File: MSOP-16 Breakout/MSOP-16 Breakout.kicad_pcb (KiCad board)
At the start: 2 copper layers, 3 parts, among them J1 Conn_01x08_Male, J2 Conn_01x08_Male, U1 LTC6820

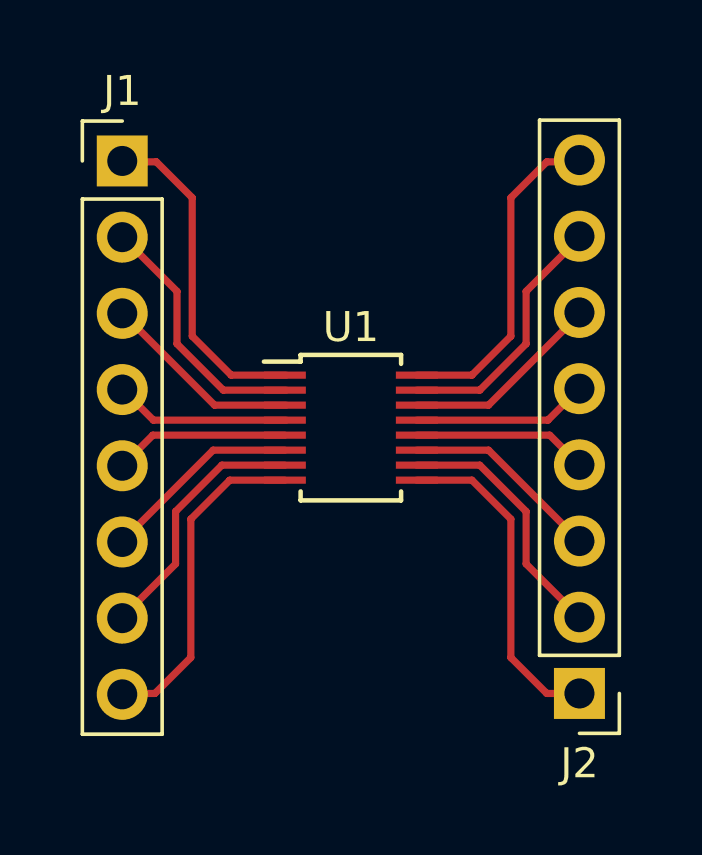
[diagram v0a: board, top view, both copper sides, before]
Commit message: Update BMS bias resistors and enable pin
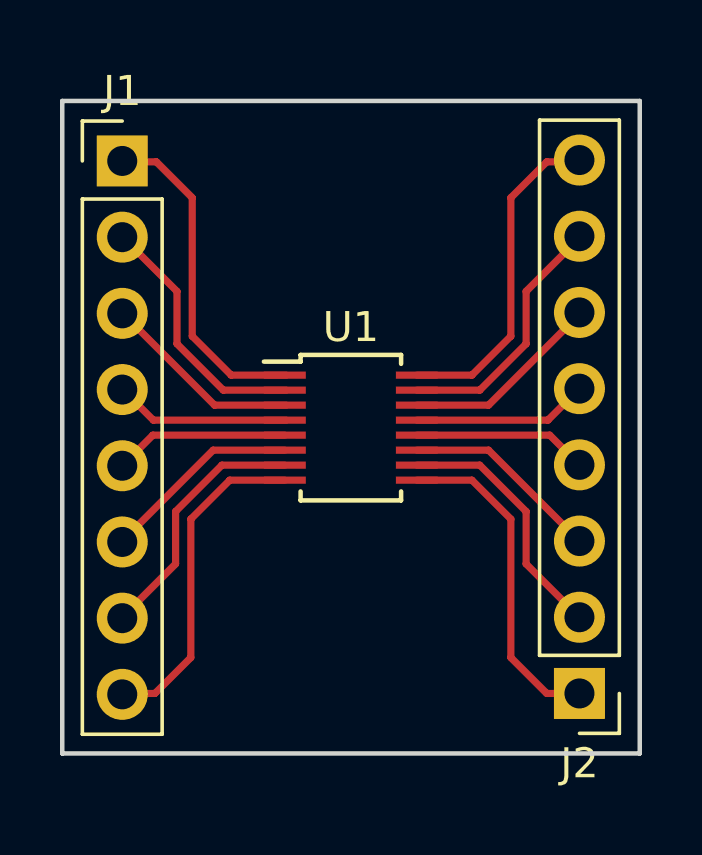
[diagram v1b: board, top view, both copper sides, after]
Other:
- board outline added: 19.3 x 21.7 mm
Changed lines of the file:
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@@
   (general
     (thickness 1.6)
-    (drawings 0)
+    (drawings 4)
     (tracks 52)
     (zones 0)
@@
     (visible_elements FFFFFF7F)
     (pcbplotparams
-      (layerselection 0x010fc_ffffffff)
+      (layerselection 0x01000_ffffffff)
       (usegerberextensions false)
       (usegerberattributes false)
@@
       (outputformat 1)
       (mirror false)
-      (drillshape 1)
+      (drillshape 0)
       (scaleselection 1)
-      (outputdirectory ""))
+      (outputdirectory "./"))
   )
   (net 0 "")
@@
     )
   )
+  (gr_line (start 23.654 43.626) (end 23.654 21.876) (layer Edge.Cuts) (width 0.15))
+  (gr_line (start 42.904 43.626) (end 23.654 43.626) (layer Edge.Cuts) (width 0.15))
+  (gr_line (start 42.904 21.876) (end 42.904 43.626) (layer Edge.Cuts) (width 0.15))
+  (gr_line (start 23.654 21.876) (end 42.904 21.876) (layer Edge.Cuts) (width 0.15))
+  (segment (start 27.986797 29.717791) (end 27.986797 25.101791) (width 0.24) (layer F.Cu) (net 1))
+  (segment (start 31.120797 31.015791) (end 29.284797 31.015791) (width 0.24) (layer F.Cu) (net 1))
+  (segment (start 29.284797 31.015791) (end 27.986797 29.717791) (width 0.24) (layer F.Cu) (net 1))
+  (segment (start 26.790797 23.905791) (end 25.700797 23.905791) (width 0.24) (layer F.Cu) (net 1))
+  (segment (start 27.986797 25.101791) (end 26.790797 23.905791) (width 0.24) (layer F.Cu) (net 1))
+  (segment (start 27.478797 29.971791) (end 27.478797 28.223791) (width 0.24) (layer F.Cu) (net 2))
+  (segment (start 29.022797 31.515791) (end 27.478797 29.971791) (width 0.24) (layer F.Cu) (net 2))
+  (segment (start 27.478797 28.223791) (end 25.700797 26.445791) (width 0.24) (layer F.Cu) (net 2))
+  (segment (start 31.120797 31.515791) (end 29.022797 31.515791) (width 0.24) (layer F.Cu) (net 2))
+  (segment (start 25.700797 28.985791) (end 28.730797 32.015791) (width 0.24) (layer F.Cu) (net 3))
+  (segment (start 28.730797 32.015791) (end 31.120797 32.015791) (width 0.24) (layer F.Cu) (net 3))
+  (segment (start 26.690797 32.515791) (end 31.120797 32.515791) (width 0.24) (layer F.Cu) (net 4))
+  (segment (start 25.700797 31.525791) (end 26.690797 32.515791) (width 0.24) (layer F.Cu) (net 4))
+  (segment (start 26.674 33.016) (end 25.654 34.036) (width 0.24) (layer F.Cu) (net 5))
+  (segment (start 31.074 33.016) (end 26.674 33.016) (width 0.24) (layer F.Cu) (net 5))
+  (segment (start 40.894 34.006) (end 39.904 33.016) (width 0.24) (layer F.Cu) (net 6))
+  (segment (start 39.904 33.016) (end 35.474 33.016) (width 0.24) (layer F.Cu) (net 6))
+  (segment (start 39.844 32.516) (end 40.894 31.466) (width 0.24) (layer F.Cu) (net 7))
+  (segment (start 35.474 32.516) (end 39.844 32.516) (width 0.24) (layer F.Cu) (net 7))
+  (segment (start 40.894 28.986) (end 37.864 32.016) (width 0.24) (layer F.Cu) (net 8))
+  (segment (start 37.864 32.016) (end 35.474 32.016) (width 0.24) (layer F.Cu) (net 8))
+  (segment (start 39.116 29.972) (end 39.116 28.224) (width 0.24) (layer F.Cu) (net 9))
+  (segment (start 37.572 31.516) (end 39.116 29.972) (width 0.24) (layer F.Cu) (net 9))
+  (segment (start 39.116 28.224) (end 40.894 26.446) (width 0.24) (layer F.Cu) (net 9))
+  (segment (start 35.474 31.516) (end 37.572 31.516) (width 0.24) (layer F.Cu) (net 9))
+  (segment (start 38.608 29.718) (end 38.608 25.102) (width 0.24) (layer F.Cu) (net 10))
+  (segment (start 35.474 31.016) (end 37.31 31.016) (width 0.24) (layer F.Cu) (net 10))
+  (segment (start 37.31 31.016) (end 38.608 29.718) (width 0.24) (layer F.Cu) (net 10))
+  (segment (start 39.804 23.906) (end 40.894 23.906) (width 0.24) (layer F.Cu) (net 10))
+  (segment (start 38.608 25.102) (end 39.804 23.906) (width 0.24) (layer F.Cu) (net 10))
   (segment (start 25.654 36.546) (end 28.684 33.516) (width 0.24) (layer F.Cu) (net 11))
   (segment (start 28.684 33.516) (end 31.074 33.516) (width 0.24) (layer F.Cu) (net 11))
@@
   (segment (start 26.744 41.626) (end 25.654 41.626) (width 0.24) (layer F.Cu) (net 13))
   (segment (start 27.94 40.43) (end 26.744 41.626) (width 0.24) (layer F.Cu) (net 13))
-  (segment (start 40.894 28.986) (end 37.864 32.016) (width 0.24) (layer F.Cu) (net 8))
-  (segment (start 37.864 32.016) (end 35.474 32.016) (width 0.24) (layer F.Cu) (net 8))
-  (segment (start 39.116 29.972) (end 39.116 28.224) (width 0.24) (layer F.Cu) (net 9))
-  (segment (start 37.572 31.516) (end 39.116 29.972) (width 0.24) (layer F.Cu) (net 9))
-  (segment (start 39.116 28.224) (end 40.894 26.446) (width 0.24) (layer F.Cu) (net 9))
-  (segment (start 35.474 31.516) (end 37.572 31.516) (width 0.24) (layer F.Cu) (net 9))
-  (segment (start 38.608 29.718) (end 38.608 25.102) (width 0.24) (layer F.Cu) (net 10))
-  (segment (start 35.474 31.016) (end 37.31 31.016) (width 0.24) (layer F.Cu) (net 10))
-  (segment (start 37.31 31.016) (end 38.608 29.718) (width 0.24) (layer F.Cu) (net 10))
-  (segment (start 39.804 23.906) (end 40.894 23.906) (width 0.24) (layer F.Cu) (net 10))
-  (segment (start 38.608 25.102) (end 39.804 23.906) (width 0.24) (layer F.Cu) (net 10))
-  (segment (start 40.894 34.006) (end 39.904 33.016) (width 0.24) (layer F.Cu) (net 6))
-  (segment (start 39.904 33.016) (end 35.474 33.016) (width 0.24) (layer F.Cu) (net 6))
-  (segment (start 26.690797 32.515791) (end 31.120797 32.515791) (width 0.24) (layer F.Cu) (net 4))
-  (segment (start 25.700797 31.525791) (end 26.690797 32.515791) (width 0.24) (layer F.Cu) (net 4))
   (segment (start 40.894 36.546) (end 37.864 33.516) (width 0.24) (layer F.Cu) (net 14))
   (segment (start 37.864 33.516) (end 35.474 33.516) (width 0.24) (layer F.Cu) (net 14))
-  (segment (start 25.700797 28.985791) (end 28.730797 32.015791) (width 0.24) (layer F.Cu) (net 3))
-  (segment (start 28.730797 32.015791) (end 31.120797 32.015791) (width 0.24) (layer F.Cu) (net 3))
   (segment (start 39.116 35.56) (end 39.116 37.308) (width 0.24) (layer F.Cu) (net 15))
   (segment (start 37.572 34.016) (end 39.116 35.56) (width 0.24) (layer F.Cu) (net 15))
   (segment (start 39.116 37.308) (end 40.894 39.086) (width 0.24) (layer F.Cu) (net 15))
   (segment (start 35.474 34.016) (end 37.572 34.016) (width 0.24) (layer F.Cu) (net 15))
-  (segment (start 27.478797 29.971791) (end 27.478797 28.223791) (width 0.24) (layer F.Cu) (net 2))
-  (segment (start 29.022797 31.515791) (end 27.478797 29.971791) (width 0.24) (layer F.Cu) (net 2))
-  (segment (start 27.478797 28.223791) (end 25.700797 26.445791) (width 0.24) (layer F.Cu) (net 2))
-  (segment (start 31.120797 31.515791) (end 29.022797 31.515791) (width 0.24) (layer F.Cu) (net 2))
   (segment (start 35.474 34.516) (end 37.31 34.516) (width 0.24) (layer F.Cu) (net 16))
   (segment (start 37.31 34.516) (end 38.608 35.814) (width 0.24) (layer F.Cu) (net 16))
@@
   (segment (start 38.608 35.814) (end 38.608 40.43) (width 0.24) (layer F.Cu) (net 16))
   (segment (start 38.608 40.43) (end 39.804 41.626) (width 0.24) (layer F.Cu) (net 16))
-  (segment (start 27.986797 29.717791) (end 27.986797 25.101791) (width 0.24) (layer F.Cu) (net 1))
-  (segment (start 31.120797 31.015791) (end 29.284797 31.015791) (width 0.24) (layer F.Cu) (net 1))
-  (segment (start 29.284797 31.015791) (end 27.986797 29.717791) (width 0.24) (layer F.Cu) (net 1))
-  (segment (start 26.790797 23.905791) (end 25.700797 23.905791) (width 0.24) (layer F.Cu) (net 1))
-  (segment (start 27.986797 25.101791) (end 26.790797 23.905791) (width 0.24) (layer F.Cu) (net 1))
-  (segment (start 26.674 33.016) (end 25.654 34.036) (width 0.24) (layer F.Cu) (net 5))
-  (segment (start 31.074 33.016) (end 26.674 33.016) (width 0.24) (layer F.Cu) (net 5))
-  (segment (start 39.844 32.516) (end 40.894 31.466) (width 0.24) (layer F.Cu) (net 7))
-  (segment (start 35.474 32.516) (end 39.844 32.516) (width 0.24) (layer F.Cu) (net 7))
 )
